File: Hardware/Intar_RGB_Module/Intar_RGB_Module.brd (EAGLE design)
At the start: 17.8 x 25.9 mm, 11 parts, among them J1 GROVE-4P-2.0-3470130P1, SW1 SWITCH_MOMENTARY

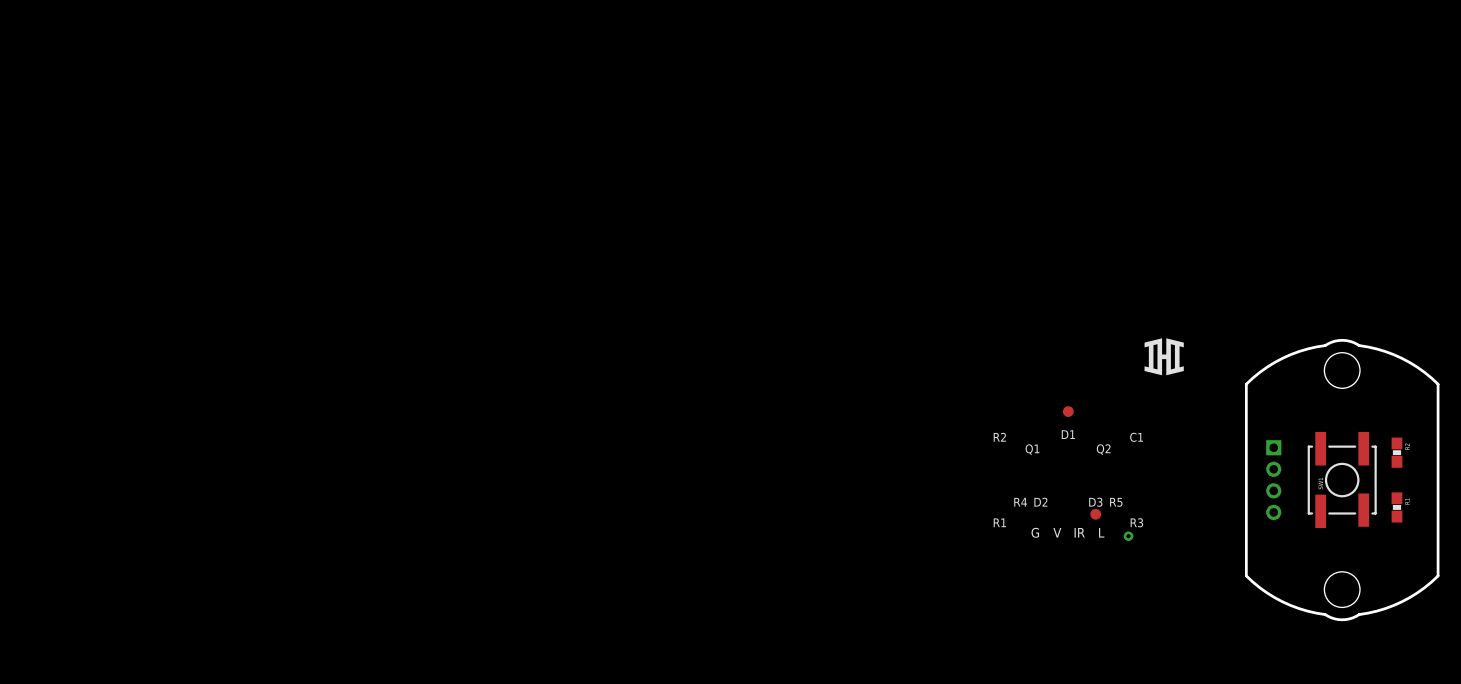
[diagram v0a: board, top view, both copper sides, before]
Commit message: Created schematics for first round of modules.
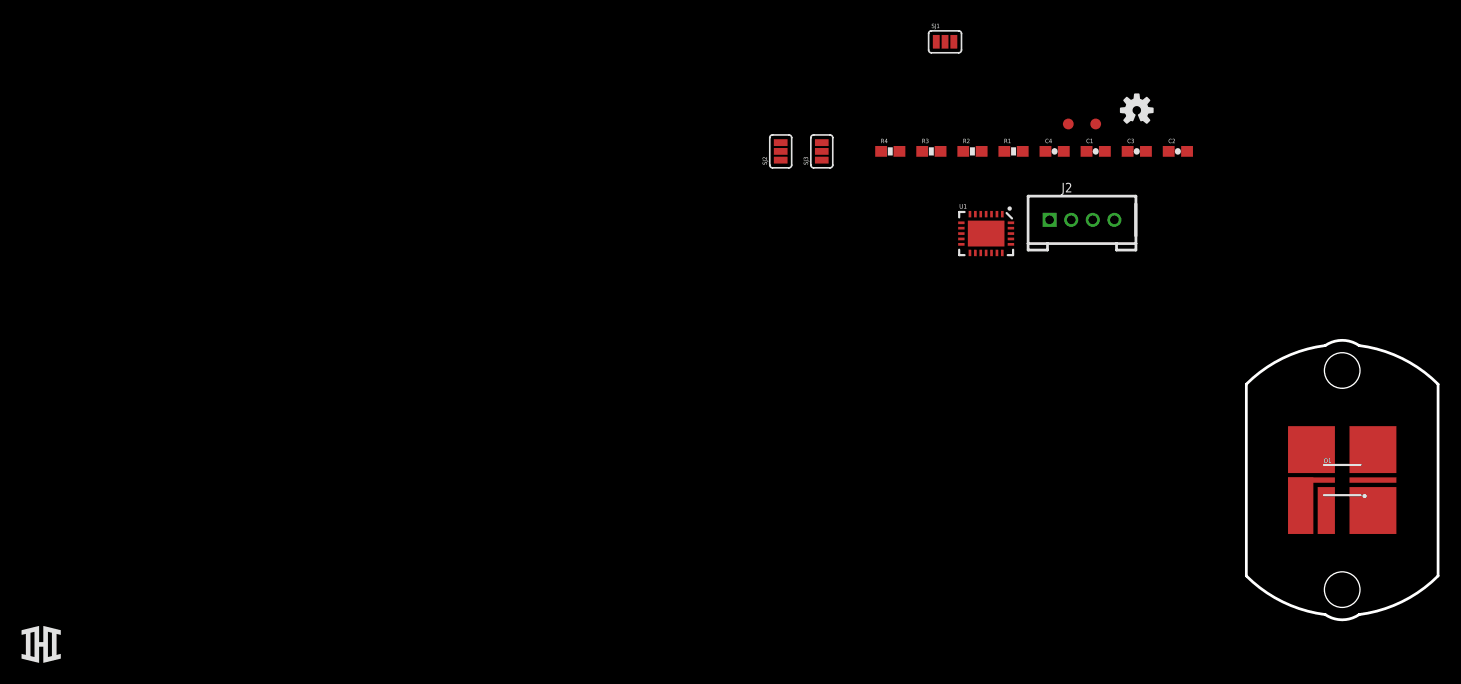
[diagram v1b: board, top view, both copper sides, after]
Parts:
- removed J1: GROVE-4P-2.0-3470130P1, Connector:4P-2.0
- removed SW1: SWITCH_MOMENTARY, Intar_Eagle_Library:KSCXXXG
- added C1, C4: 1.0uF, SparkFun-Capacitors:0603-CAP
- added C2, C3: 0.047uF, SparkFun-Capacitors:0603-CAP
- added D1: LED_RGB_6PASMT, Intar_Eagle_Library:ASMT-YTB7-0AA02
- added J2: GROVE-4P-2.0-3470130P1, Connector:4P-2.0
- added R3, R4: 10K, SparkFun-Resistors:0603-RES
- added SJ1: (no value), SparkFun-Retired:SJ_3_PASTE1&2&3
- added SJ2, SJ3: (no value), SparkFun-Retired:SJ_3_PASTE2&3
- added U1: LP5521LONG, Intar_Eagle_Library:WQFN-24_LONG
- R1: value 10K -> 4.7K
- R2: value 100 -> 4.7K
- moved U$1 107.5 mm to (-120.7, -15.2)
- moved FRAME1 76.7 mm to (-101.6, 11.4)
- moved R1 48.5 mm to (-30.5, 30.5), turned to 0 degrees
- moved R2 48.3 mm to (-34.3, 30.5), turned to 0 degrees
- moved LOGO1 47.3 mm to (-19.1, 34.3), flipped to the top
- moved FID2 36.3 mm to (-25.4, 33.0)
- moved FID1 26.8 mm to (-22.9, 33.0)
- moved STANDOFF1 20.3 mm to (0.00, 10.2)
- moved STANDOFF2 20.3 mm to (0.00, -10.2)
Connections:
- removed net BTN: J1.1, R2.1
- new net B: D1.6, U1.19
- new net G: D1.5, U1.18
- new net N$10: R4.1, SJ3.1
- new net N$2: C2.2, U1.24
- new net N$3: C3.1, U1.1
- new net N$4: C3.2, U1.23
- new net N$5: C4.1, U1.22
- new net N$6: R1.2, SJ1.3
- new net N$7: R2.2, SJ1.1
- new net N$9: R3.1, SJ2.1
- new net R: D1.4, U1.17
- new net SCL: J2.4, R2.1, U1.15
- new net SDA: J2.3, R1.1, U1.13
- new net SEL0: SJ2.2, U1.20
- new net SEL1: SJ3.2, U1.21
- net GND: now also C1.2, C4.2, D1.1, D1.2, D1.3, J2.1, SJ2.3, SJ3.3, U1.4, U1.5, U1.7, U1.PAD; no longer J1.4, SW1.3, SW1.4
- net N$1: now also C2.1, U1.2; no longer R1.1, R2.2, SW1.1, SW1.2
- net VCC: now also C1.1, J2.2, R3.2, R4.2, SJ1.2, U1.14, U1.3; no longer J1.3, R1.2
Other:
- board text removed: "C1"
- board text removed: "D1"
- board text removed: "D2"
- board text removed: "D3"
- board text removed: "G"
- board text removed: "IR"
- board text removed: "Intar IR LED Module"
- board text removed: "L"
- board text removed: "Q1"
- board text removed: "Q2"
- board text removed: "R1"
- board text removed: "R2"
- board text removed: "R3"
- board text removed: "R4"
- board text removed: "R5"
- board text removed: "Shawn Hymel"
- board text removed: "V"
- board text removed: "Visible LEDs"
- board text removed: "v01"

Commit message: Arranged components on all modules
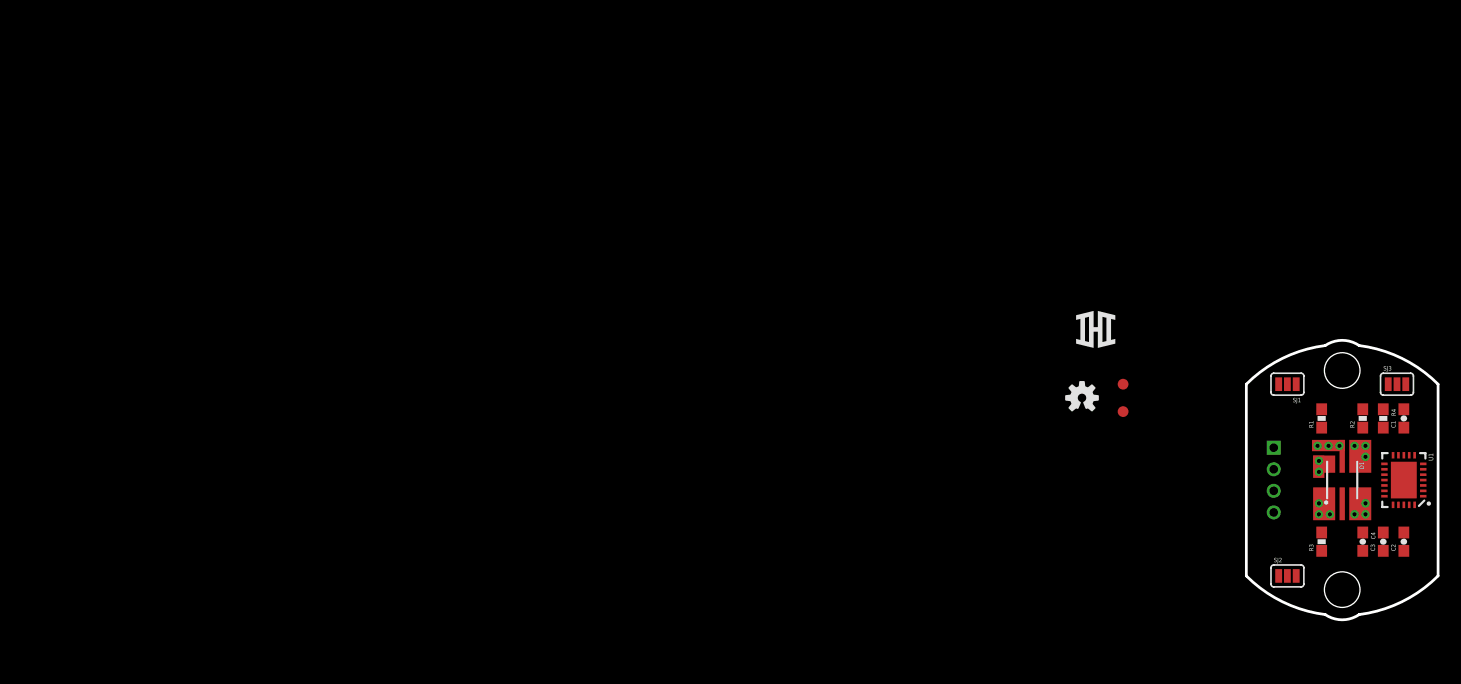
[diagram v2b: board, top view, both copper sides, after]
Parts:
- D1: value LED_RGB_6PASMT -> LED_RGB_6PASMT_M; device Intar_Eagle_Library:ASMT-YTB7-0AA02 -> Intar_Eagle_Library:ASMT-YTB7-0AA02_M
- moved U$1 102.1 mm to (-22.9, 14.0)
- moved FRAME1 76.7 mm to (-33.0, -22.9)
- moved SJ2 61.3 mm to (-5.08, -8.89), turned to 0 degrees
- moved SJ3 57.5 mm to (5.08, 8.89), turned to 0 degrees
- moved R4 52.0 mm to (3.81, 5.71), turned to 270 degrees
- moved R3 51.2 mm to (-1.91, -5.71), turned to 90 degrees
- moved C4 46.1 mm to (1.91, -5.71), turned to 270 degrees
- moved U1 45.0 mm to (5.71, 0.00), turned to 270 degrees
- moved SJ1 44.9 mm to (-5.08, 8.89), turned to 180 degrees
- moved R2 43.9 mm to (1.91, 5.71), turned to 90 degrees
- moved C3 42.8 mm to (3.81, -5.71), turned to 90 degrees
- moved C2 41.8 mm to (5.71, -5.71), turned to 90 degrees
- moved C1 37.8 mm to (5.71, 5.71), turned to 90 degrees
- moved R1 37.8 mm to (-1.91, 5.71), turned to 90 degrees
- moved J2 30.0 mm to (-6.35, 0.00), flipped to the bottom, turned to 270 degrees
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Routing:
- added copper zone on layer 16, net B

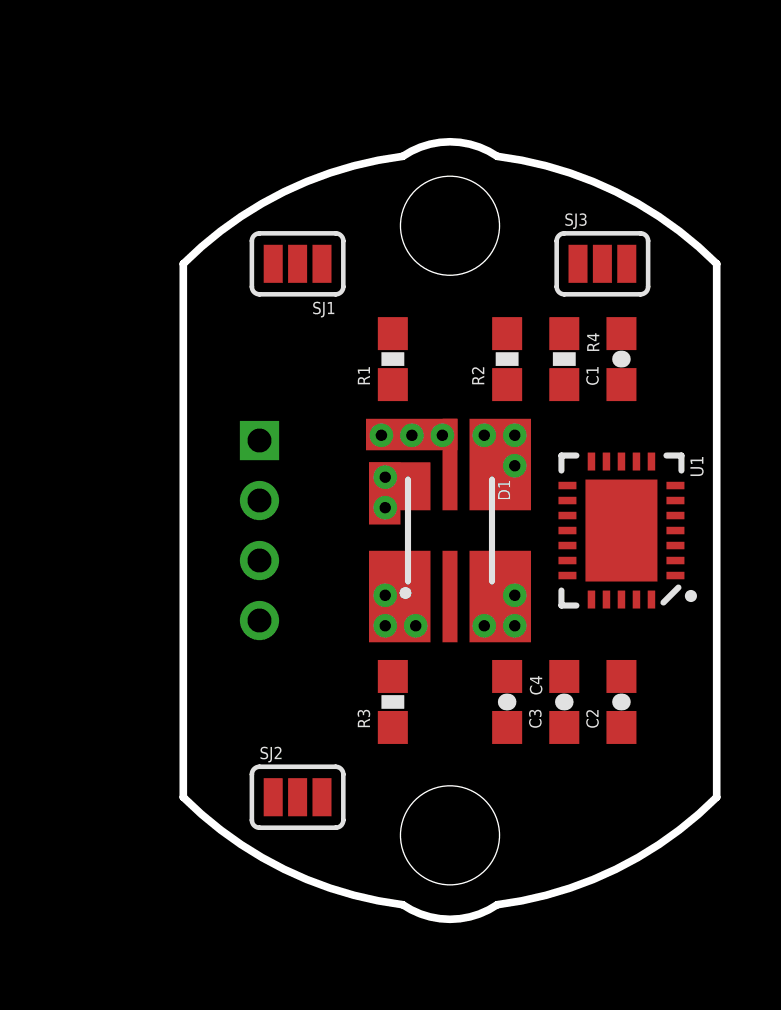
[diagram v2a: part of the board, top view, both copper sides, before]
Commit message: RGB layout almost done'
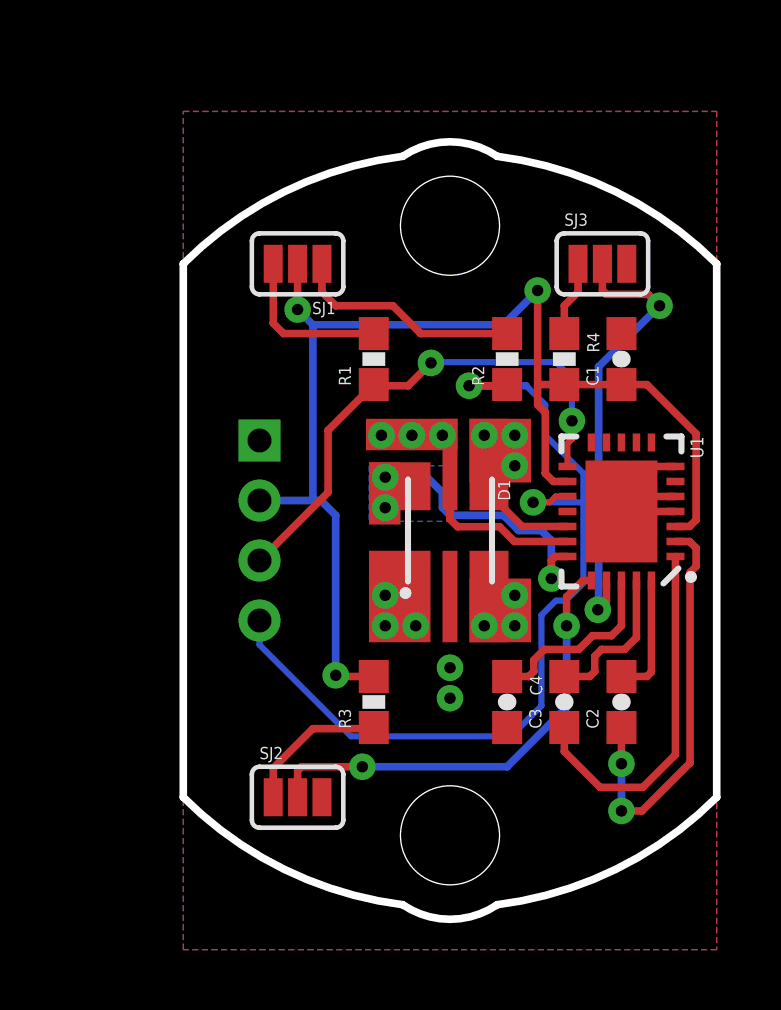
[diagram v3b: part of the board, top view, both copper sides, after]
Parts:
- moved R1 0.64 mm to (-2.54, 5.71)
- moved R3 0.64 mm to (-2.54, -5.71)
- moved U1 0.64 mm to (5.71, 0.64)
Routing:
- net VCC: track 0.00 -> 42.1 mm, vias 0 -> 3
- net SCL: track 0.00 -> 30.2 mm, vias 0 -> 2
- net SDA: track 0.00 -> 17.6 mm, vias 0 -> 2
- net SEL0: track 0.00 -> 15.5 mm, vias 0 -> 2
- net SEL1: track 0.00 -> 15.1 mm, vias 0 -> 2
- net N$1: track 0.00 -> 13.8 mm, vias 0 -> 2
- net N$3: track 0.00 -> 12.1 mm
- net B: track 0.00 -> 9.79 mm, vias 2 -> 3
- net N$7: track 0.00 -> 7.69 mm
- net GND: track 0.00 -> 7.28 mm, vias 0 -> 8
- net G: track 0.00 -> 7.12 mm, vias 0 -> 3
- net N$5: track 0.00 -> 6.24 mm
- net N$6: track 0.00 -> 5.48 mm
- net N$4: track 0.00 -> 5.14 mm
- net R: track 0.00 -> 4.93 mm, vias 0 -> 3
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- added copper zone on layer 16, net G
- added copper zone on layer 1, net GND
- added copper zone on layer 16, net GND
- added copper zone on layer 16, net R

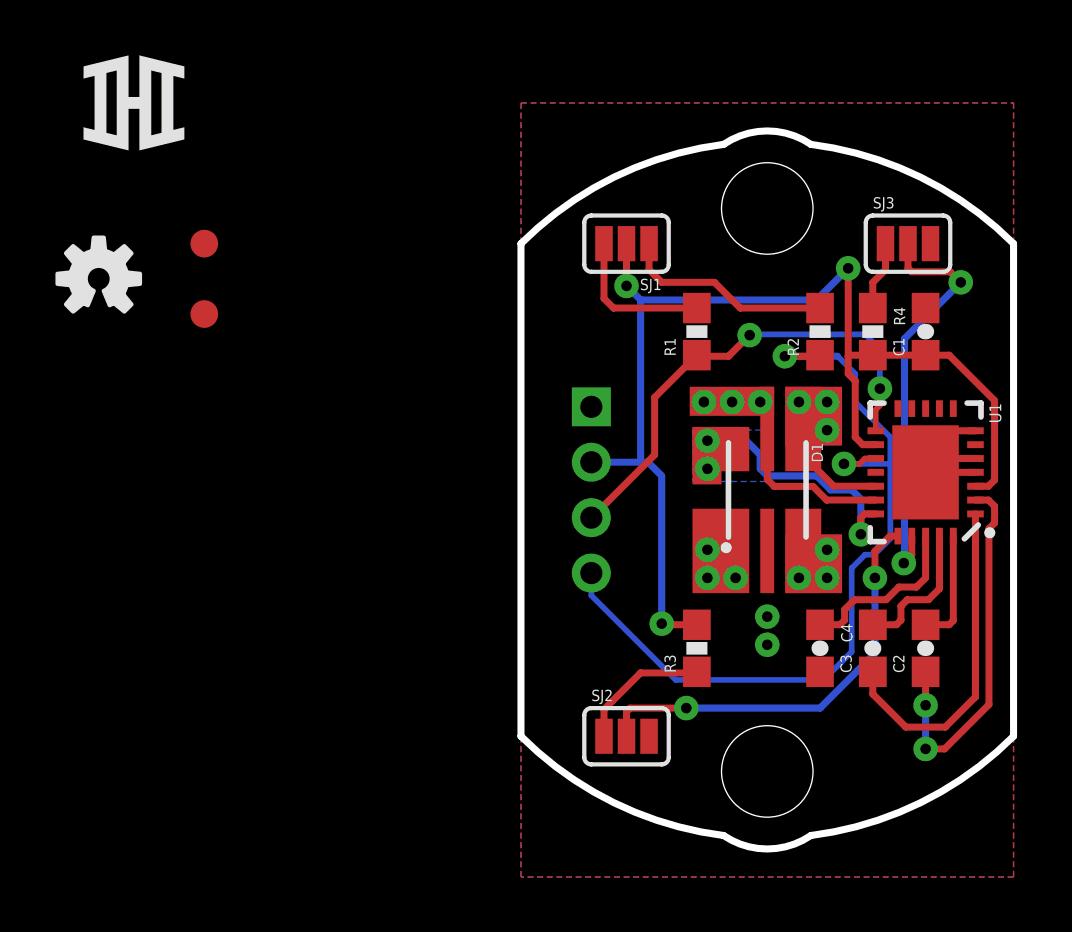
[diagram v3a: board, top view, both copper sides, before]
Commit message: Finished RGB and IR modules
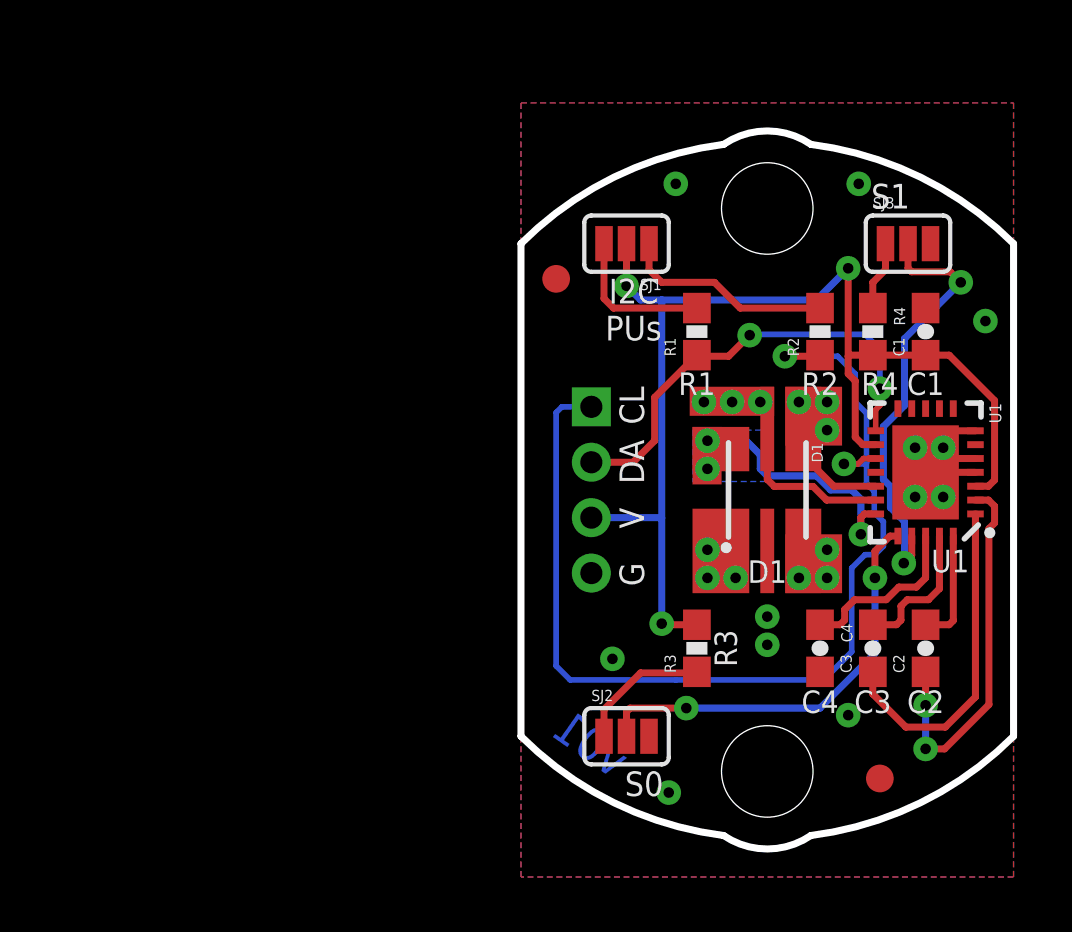
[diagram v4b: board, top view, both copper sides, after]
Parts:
- moved U$1 35.7 mm to (5.08, -8.26), flipped to the bottom, turned to 270 degrees
- moved FID2 29.6 mm to (4.06, -10.4)
- moved LOGO1 29.2 mm to (5.08, 8.26), flipped to the bottom, turned to 270 degrees
- moved FID1 12.8 mm to (-7.62, 7.62)
- renumbered J2 to J1
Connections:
- net GND: now also J1.4; no longer J1.1
- net SCL: now also J1.1; no longer J1.4
- net SDA: now also J1.2; no longer J1.3
- net VCC: now also J1.3; no longer J1.2
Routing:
- net SCL: track 30.2 -> 39.1 mm
- net SDA: track 17.6 -> 16.5 mm
- net SEL1: track 15.1 -> 15.7 mm
- net GND: vias 8 -> 18
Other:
- board text added: "C1"
- board text added: "C2"
- board text added: "C3"
- board text added: "C4"
- board text added: "CL"
- board text added: "D1"
- board text added: "DA"
- board text added: "G"
- board text added: "I2C PUs"
- board text added: "Intar RGB Module"
- board text added: "R1"
- board text added: "R2"
- board text added: "R3"
- board text added: "R4"
- board text added: "S0"
- board text added: "S1"
- board text added: "Shawn Hymel"
- board text added: "U1"
- board text added: "V"
- board text added: "v01"

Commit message: Moved IHI and OSH logos away from name on all boards.
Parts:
- moved LOGO1 0.63 mm to (4.45, 8.26)
- moved U$1 0.63 mm to (4.45, -8.26)
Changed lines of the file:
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@@
 <setting verticaltext="up"/>
 </settings>
-<grid distance="0.01" unitdist="inch" unit="inch" style="dots" multiple="1" display="yes" altdistance="0.005" altunitdist="inch" altunit="inch"/>
+<grid distance="0.05" unitdist="inch" unit="inch" style="dots" multiple="1" display="yes" altdistance="0.005" altunitdist="inch" altunit="inch"/>
 <layers>
 <layer number="1" name="Top" color="4" fill="1" visible="yes" active="yes"/>
@@
 <element name="FID2" library="SparkFun-Aesthetics" package="FIDUCIAL-1X2" value="FIDUCIAL1X2" x="4.064" y="-10.414"/>
 <element name="FRAME1" library="SparkFun-Aesthetics" package="CREATIVE_COMMONS" value="FRAME-LETTER" x="-33.02" y="-22.86"/>
-<element name="LOGO1" library="SparkFun-Aesthetics" package="OSHW-LOGO-S" value="OSHW-LOGOS" x="5.08" y="8.255" rot="MR270"/>
+<element name="LOGO1" library="SparkFun-Aesthetics" package="OSHW-LOGO-S" value="OSHW-LOGOS" x="4.445" y="8.255" rot="MR270"/>
 <element name="R1" library="SparkFun-Resistors" package="0603-RES" value="4.7K" x="-2.54" y="5.715" rot="R90">
 <attribute name="PROD_ID" value="RES-07857" x="-2.54" y="5.715" size="1.778" layer="27" rot="R90" display="off"/>
@@
 <element name="STANDOFF2" library="SparkFun-Electromechanical" package="STAND-OFF" value="STAND-OFF" x="0" y="-10.16"/>
 <element name="U1" library="Intar_Eagle_Library" package="WQFN-24_LONG" value="LP5521LONG" x="5.715" y="0.635" rot="R270"/>
-<element name="U$1" library="Intar_Eagle_Library" package="LOGO_SM" value="LOGOSM" x="5.08" y="-8.255" rot="MR270"/>
+<element name="U$1" library="Intar_Eagle_Library" package="LOGO_SM" value="LOGOSM" x="4.445" y="-8.255" rot="MR270"/>
 <element name="J1" library="Connector" package="4P-2.0" value="GROVE-4P-2.0-3470130P1" x="-6.35" y="0" rot="MR270"/>
 </elements>
